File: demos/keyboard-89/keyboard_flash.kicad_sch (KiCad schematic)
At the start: 1 part, among them U3 GD25Q16E

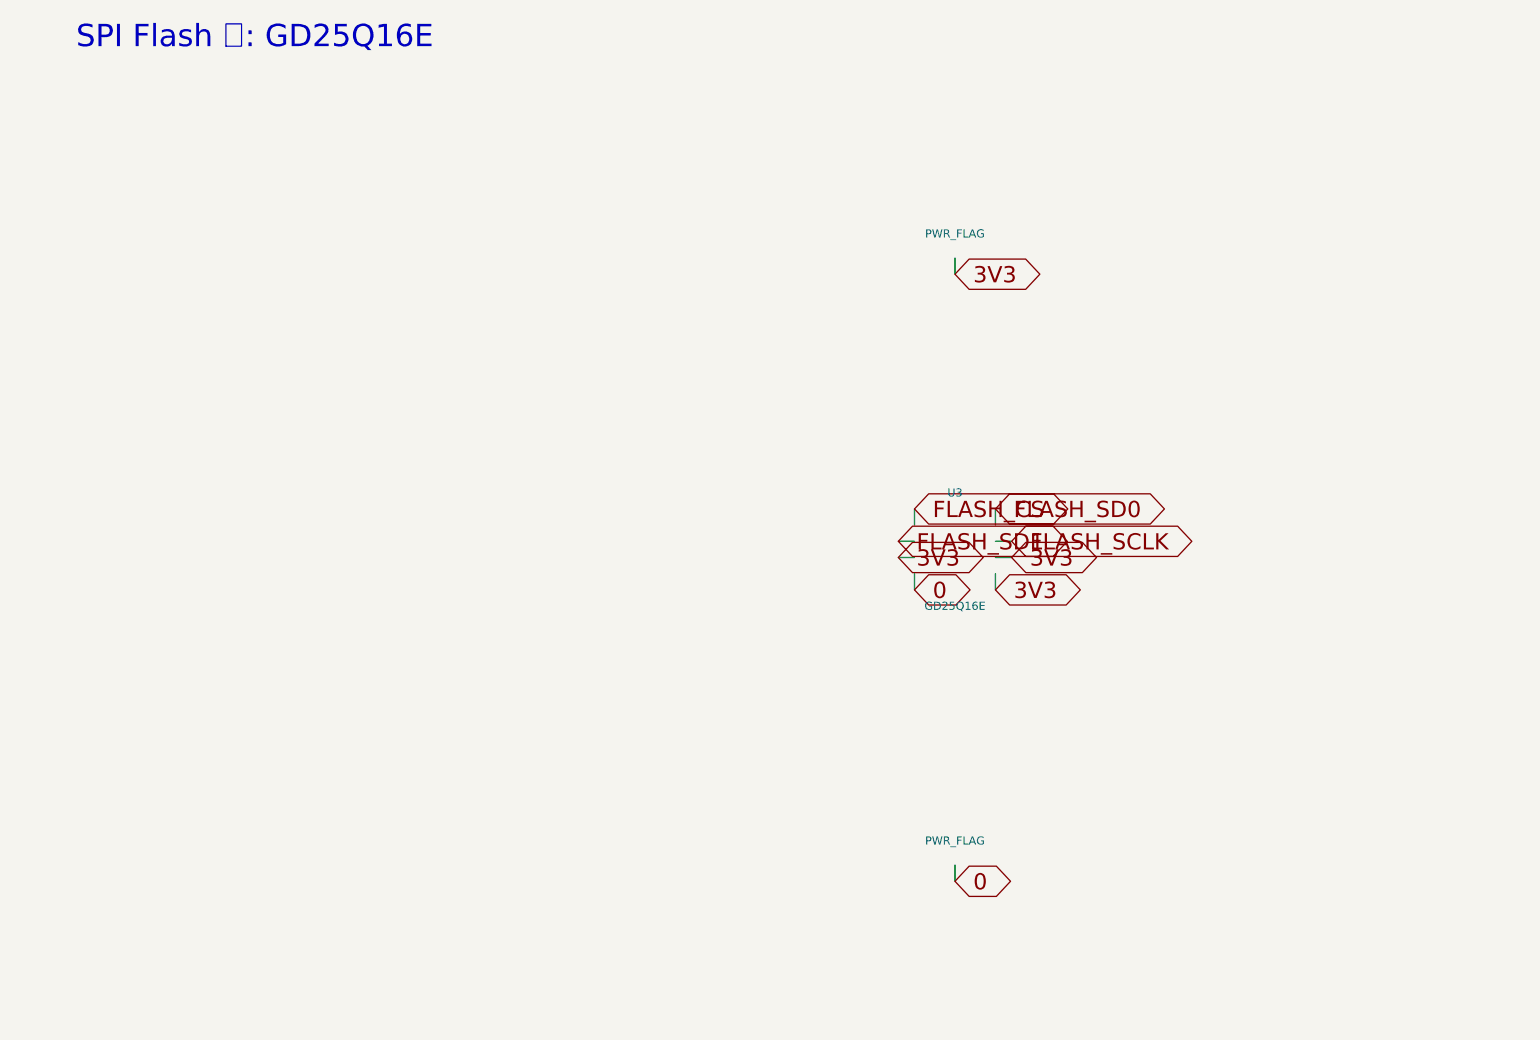
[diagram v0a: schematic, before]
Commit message: fix: update default label height in kicad_sch_add_label function to 1.27mm
feat: add redraw_kb89.py script for redrawing keyboard-89 schematic with new tools
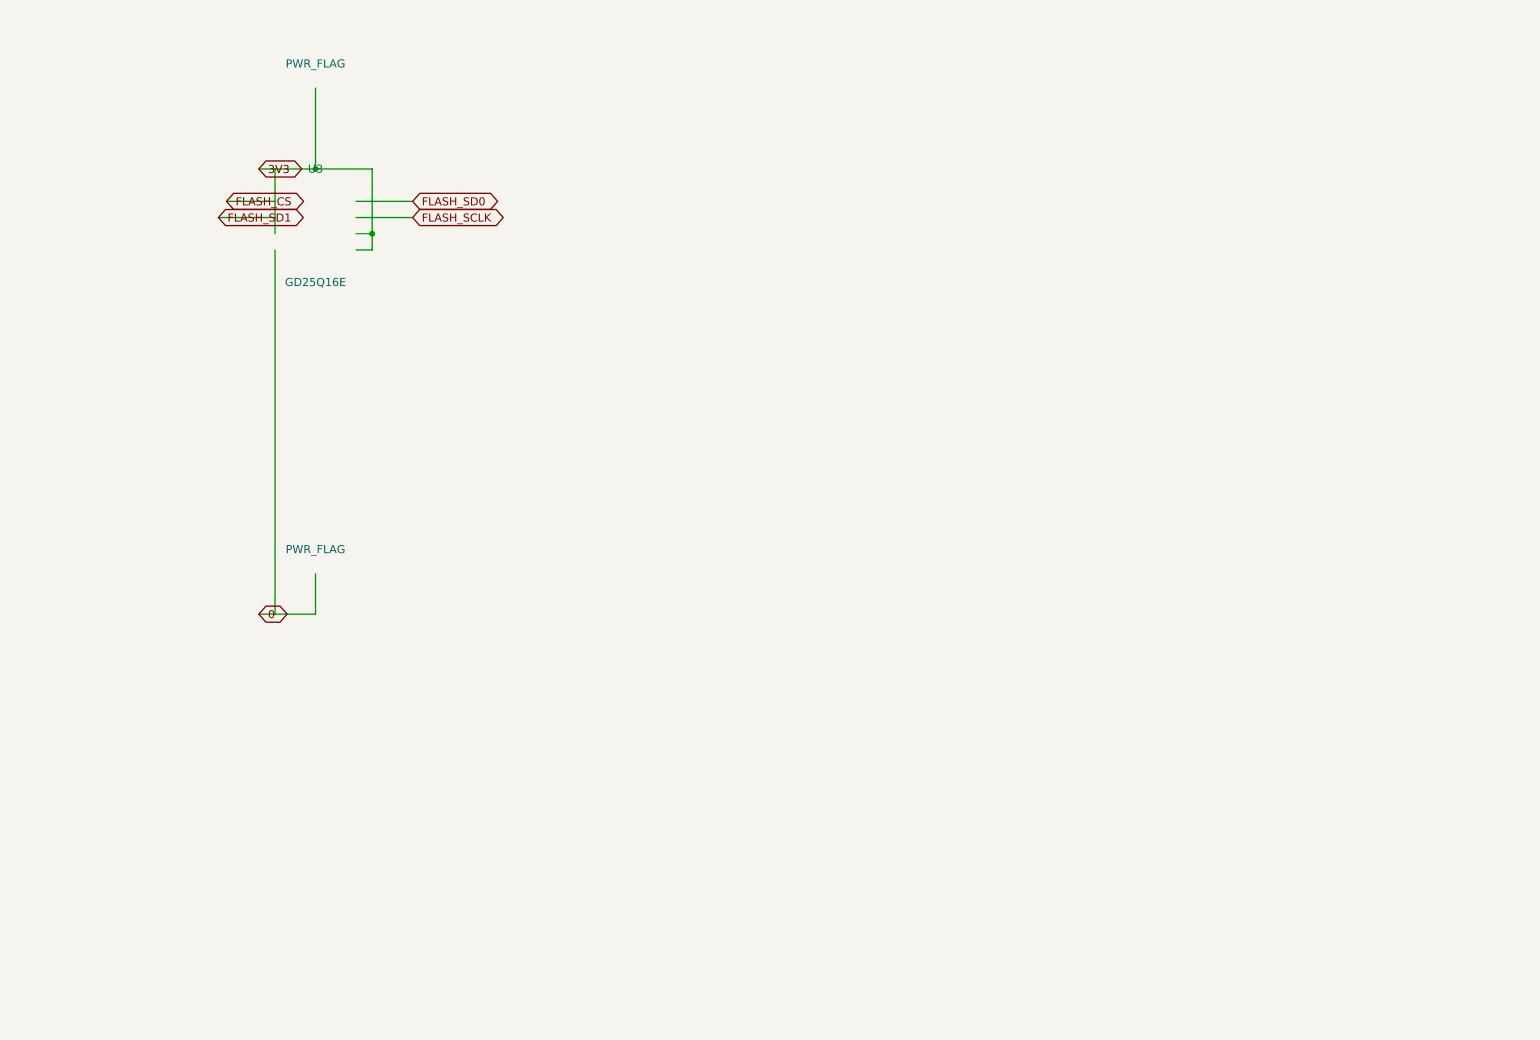
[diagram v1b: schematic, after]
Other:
- note removed: "SPI Flash 页: GD25Q16E"

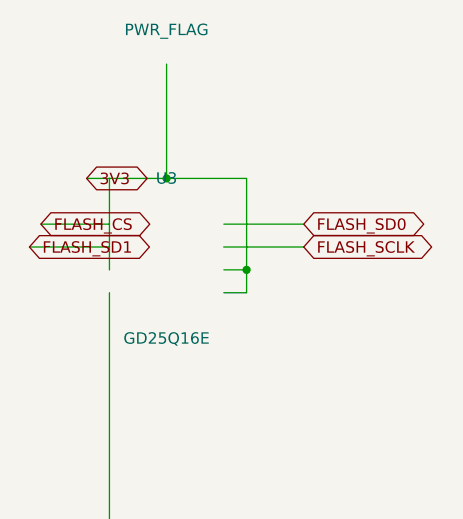
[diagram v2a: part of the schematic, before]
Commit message: feat: add overlap checking and auto repositioning tools
- Introduced a new module for checking and fixing overlaps and out-of-bounds elements in schematic designs.
- Implemented functions to read existing wires and check for overlaps between symbols and labels.
- Enhanced label placement logic to avoid collisions with existing wires.
- Updated the circuit drawing function to utilize the new overlap checking features.
- Modified the redraw tests to accommodate changes in label spacing and positioning.
- Added new tools to the main tools list for easy access.
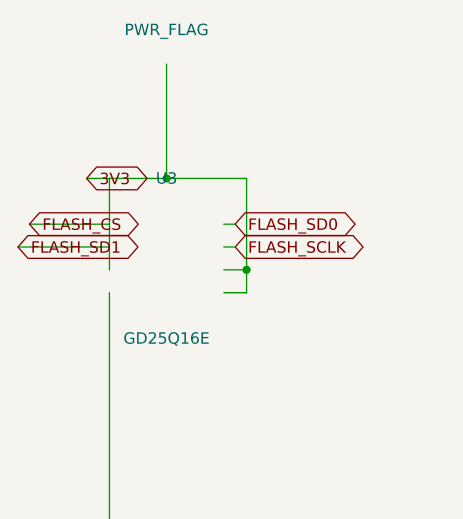
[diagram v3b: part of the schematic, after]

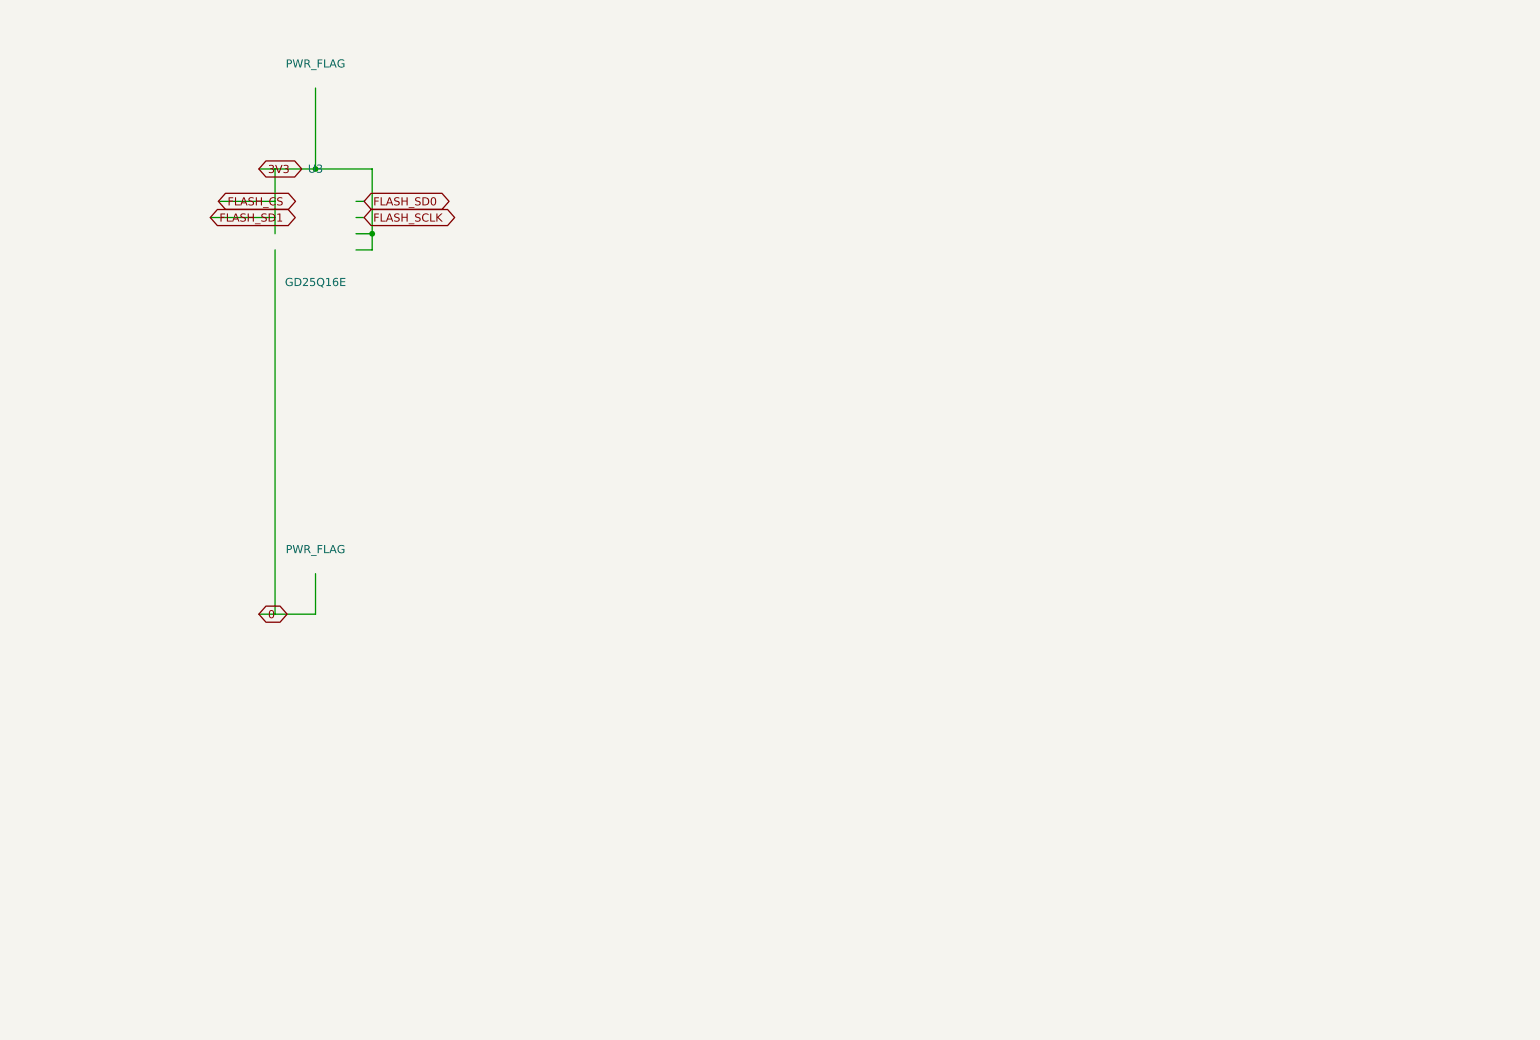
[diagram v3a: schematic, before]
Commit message: Add ERC report, AI setup documentation, and bootstrap scripts
- Created a new ERC report for the keyboard-89 project detailing isolated pin labels and library issues.
- Added AI environment bootstrap documentation for setting up the development environment on Windows and Linux.
- Implemented a PowerShell bootstrap script for Windows to automate the setup of dependencies, environment, and build process.
- Developed a corresponding bash bootstrap script for Linux with similar functionality.
- Introduced a new test for verifying pin connections in the symbol writer module.
- Added JSON report for failed drawing processes with a specific error message in Chinese.
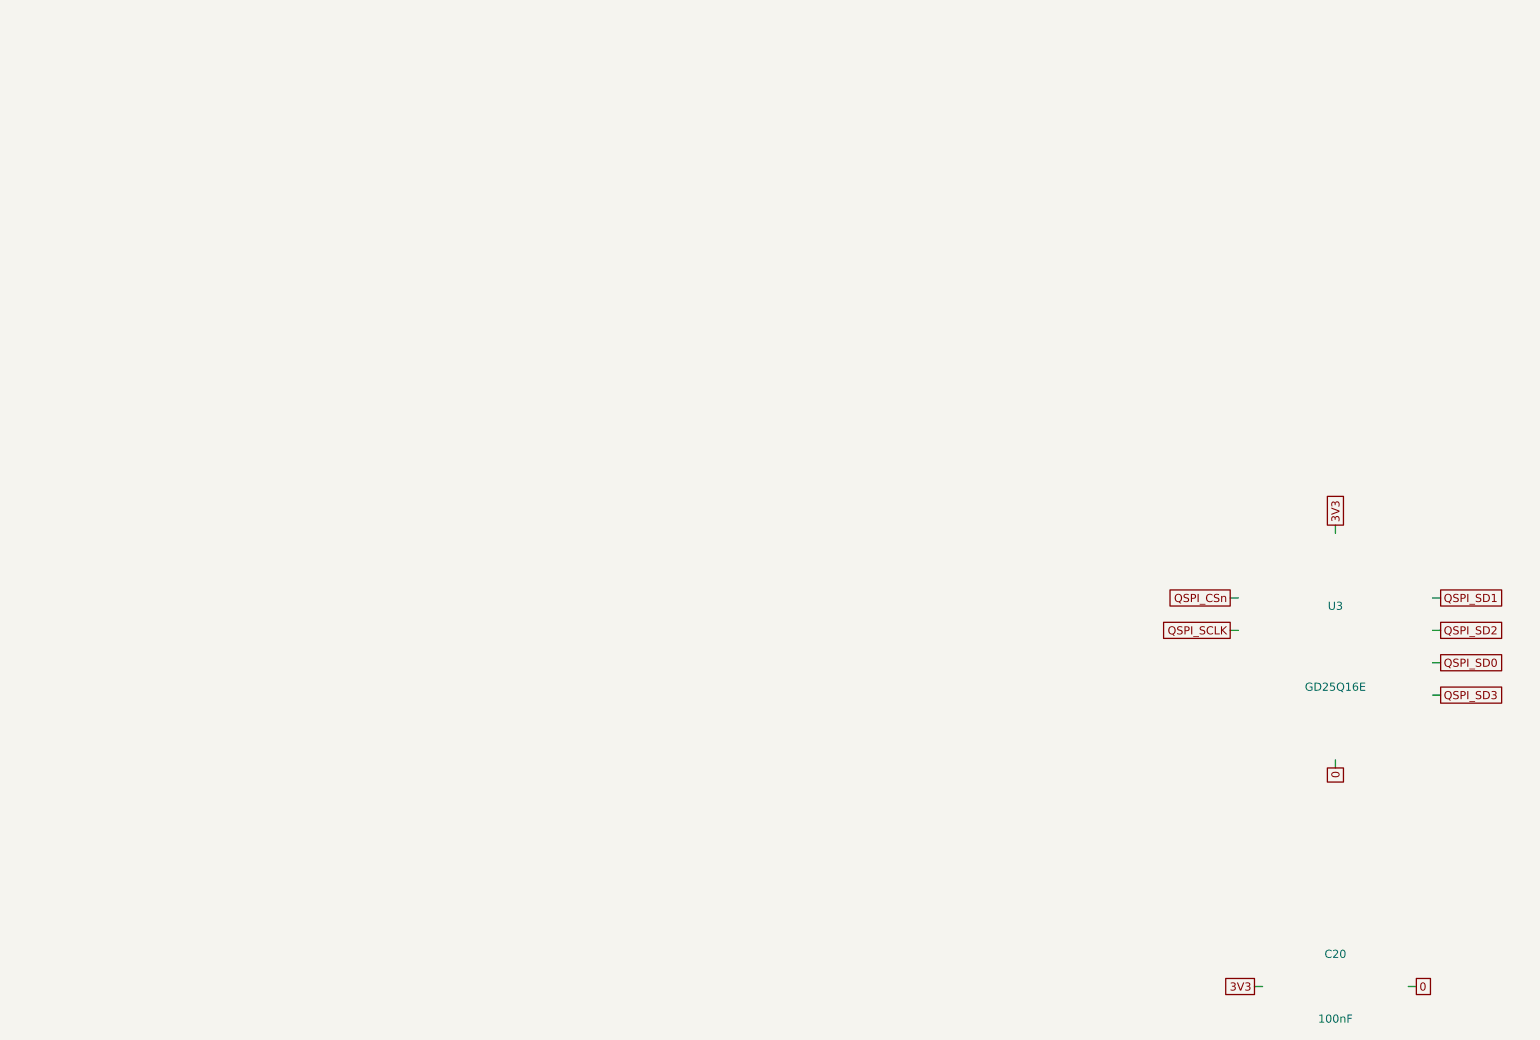
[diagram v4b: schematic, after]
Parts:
- added C20: 100nF, keyboard-89_local:C_0402_1005Metric, symbol keyboard-89_local:C_GENERIC
- U3: footprint Package_SO:SOIC-8_3.9x4.9mm_P1.27mm -> keyboard-89_local:SOIC-8_3.9x4.9mm_P1.27mm
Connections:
- net 0: now also C20.2
- net 3V3: now also C20.1; no longer U3.3 (WP#), U3.7 (HOLD#)
- net FLASH_CS renamed QSPI_CSn
- net FLASH_SCLK renamed QSPI_SCLK
- net FLASH_SD0 renamed QSPI_SD0
- net FLASH_SD1 renamed QSPI_SD1
- new net QSPI_SD2: U3.3 (IO2)
- new net QSPI_SD3: U3.7 (IO3)
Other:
- company: (none) -> Keyboard-89
- title: keyboard_flash -> Keyboard-89 QSPI Flash
